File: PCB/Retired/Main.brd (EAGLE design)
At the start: 73 x 61 mm, 4 parts, among them U1 ESP32DEVKITC

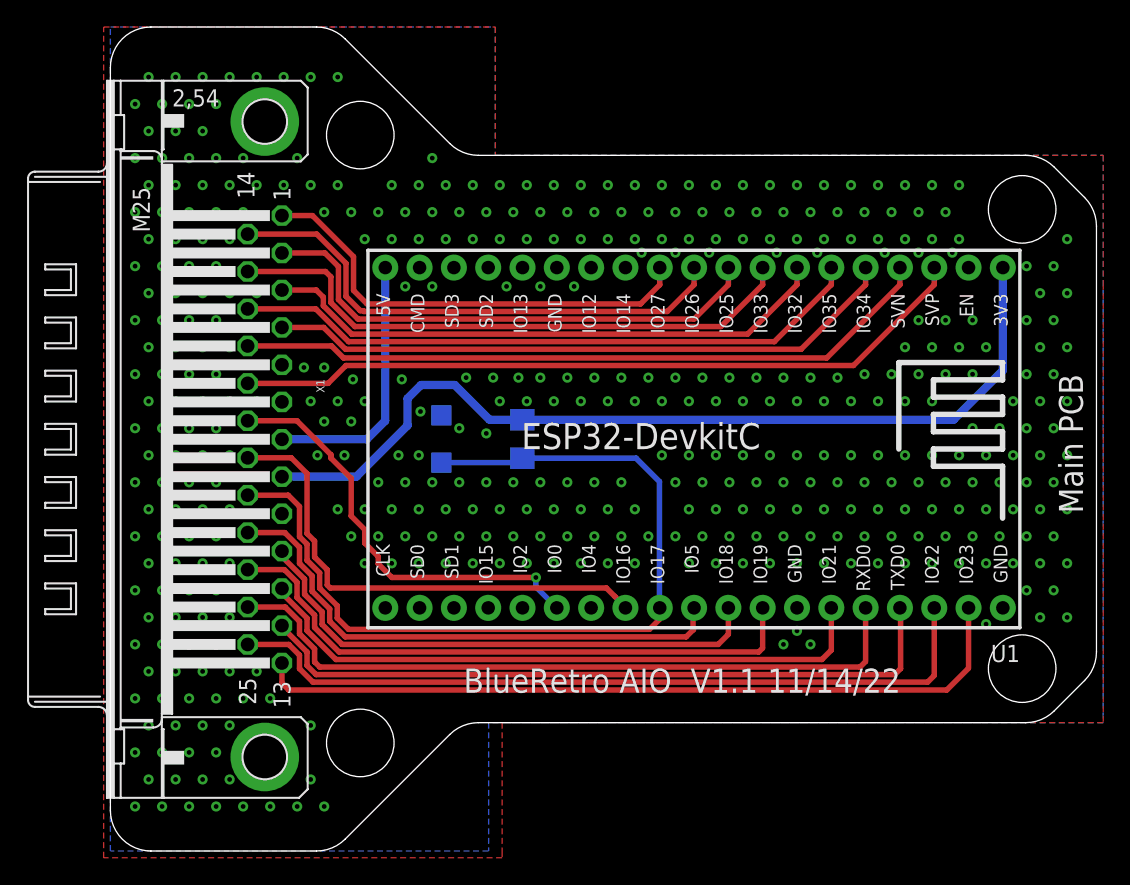
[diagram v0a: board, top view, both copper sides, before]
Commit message: Retiring Main PCB
Retiring Original Main PCB design as the unit is thinner that the standard footprint.  This was causing  confusion.  The new main used to be Main Alt Wide version.  It is now the standard as it fits the standard ESP footprint.  The Thinner version has been moved to the retired folder in PCBs
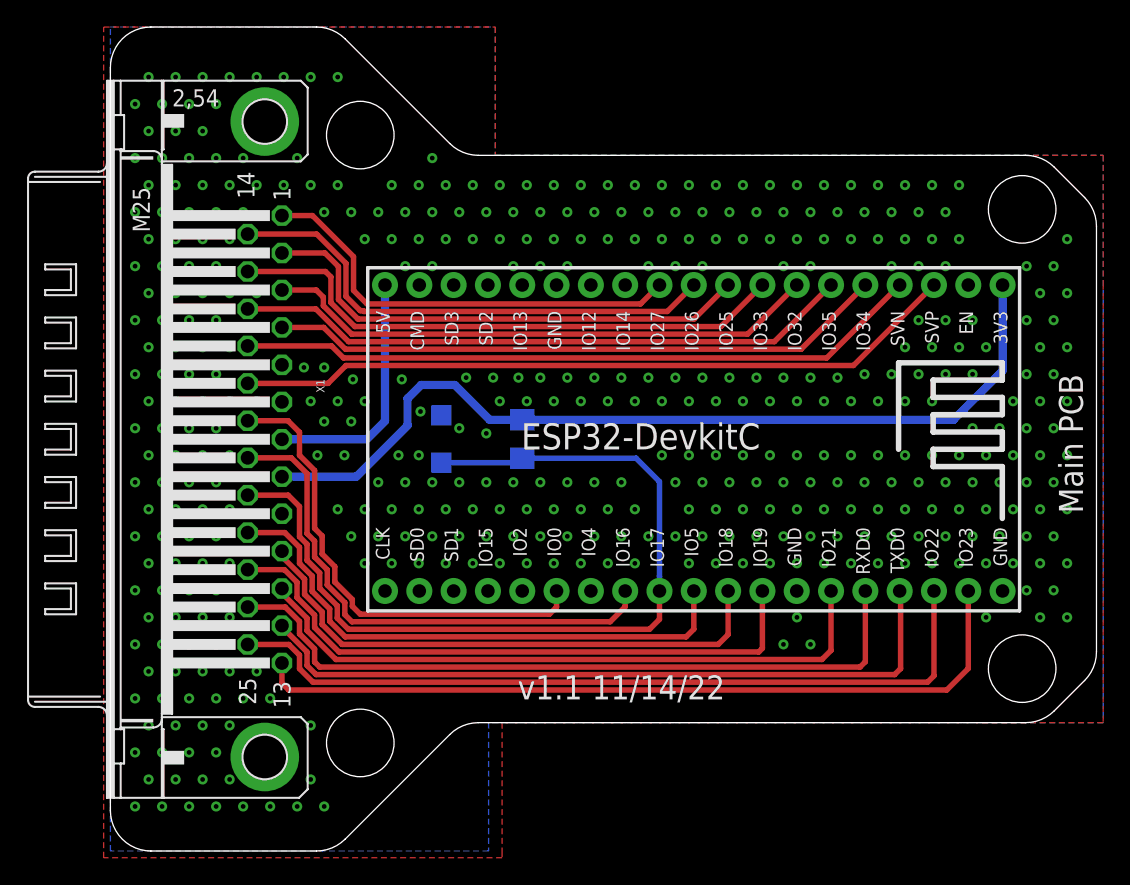
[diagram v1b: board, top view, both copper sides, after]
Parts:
- U1: device ESP32-DEVKITC4:ESP32-DEVKITC -> ESP32-DEVKITC:ESP32-DEVKITC
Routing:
- net IO0: track 31.7 -> 35.5 mm, vias 1 -> 0
- net IO16: track 36.5 -> 39.1 mm
- net 3V3IN: track 67.6 -> 66.3 mm
- net 5VIN: track 19.6 -> 18.3 mm
- net IO39: track 52.2 -> 50.9 mm
- net IO36: track 55.1 -> 53.8 mm
- net IO33: track 43.5 -> 42.2 mm
- net IO25: track 38.8 -> 37.5 mm
- net IO35: track 47.2 -> 45.9 mm
- net IO34: track 47.1 -> 45.8 mm
- net IO32: track 42.6 -> 41.3 mm
- net IO27: track 34.0 -> 32.7 mm
- net IO26: track 38.9 -> 37.6 mm
- net IO1: track 52.6 -> 53.9 mm
- net IO3: track 52.8 -> 54.1 mm
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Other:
- board text added: "v1.1 11/14/22"
- board text removed: "BlueRetro AIO V1.1 11/14/22"
